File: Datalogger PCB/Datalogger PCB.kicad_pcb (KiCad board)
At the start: 2 copper layers, 9 parts, among them J1 Conn_01x02_Pin, U2 W25Q128JVS

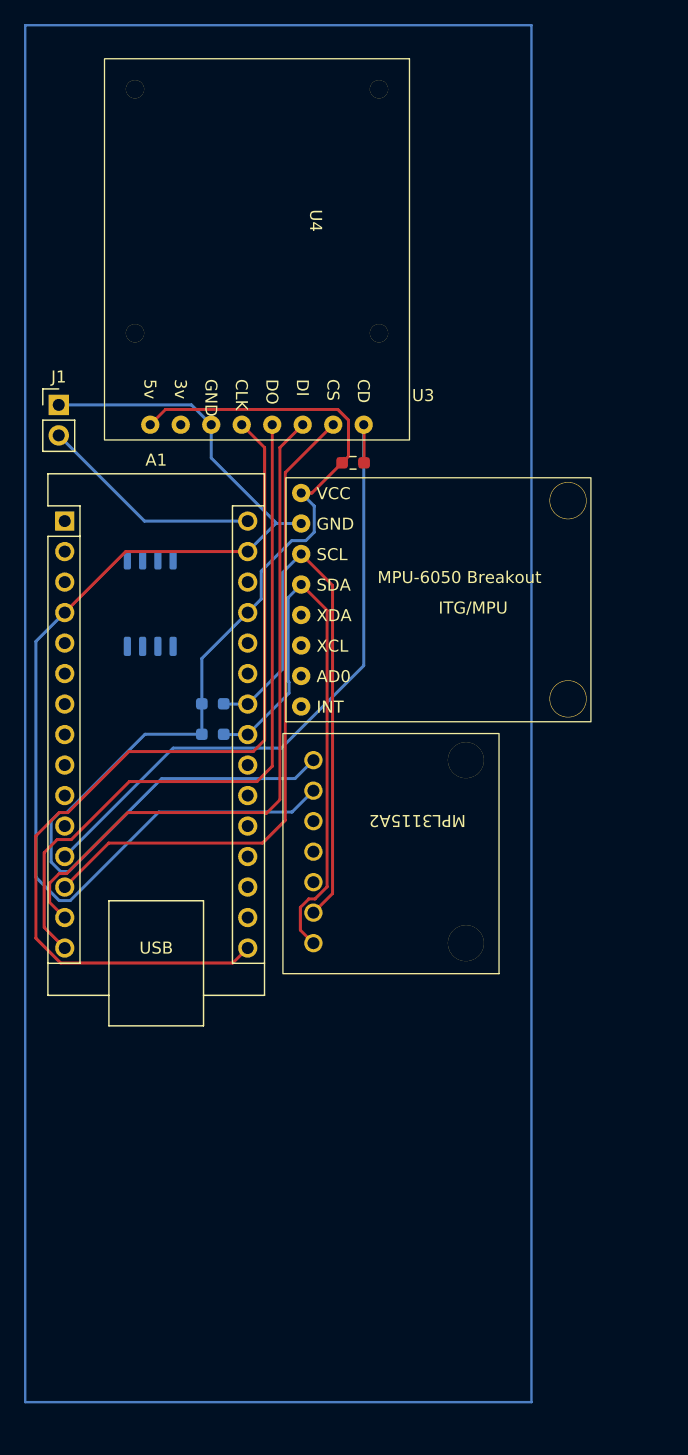
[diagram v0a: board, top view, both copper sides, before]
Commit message: Turn Schematic into PCB
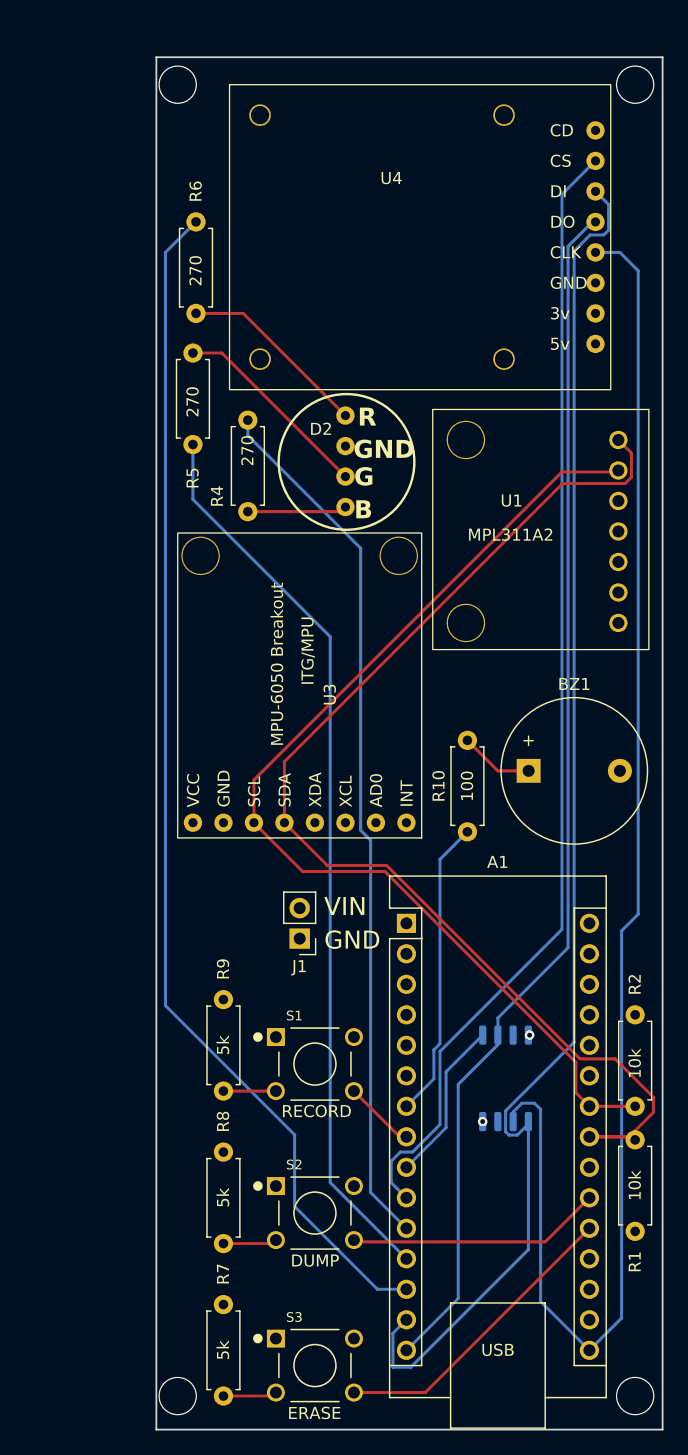
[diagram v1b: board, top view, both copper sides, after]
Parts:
- removed R3: 10k, Resistor_SMD:R_0603_1608Metric_Pad0.98x0.95mm_HandSolder
- added BZ1: Buzzer, Buzzer_Beeper:Buzzer_12x9.5RM7.6, F.Cu at (102.9, 82.5)
- added D2: LED_RKGB, Breakout Boards:RGB_LED, F.Cu at (87.6, 53.0)
- added R10: 100, Resistor_THT:R_Axial_DIN0207_L6.3mm_D2.5mm_P7.62mm_Horizontal, F.Cu at (97.8, 87.6)
- added R4: 270, Resistor_THT:R_Axial_DIN0207_L6.3mm_D2.5mm_P7.62mm_Horizontal, F.Cu at (79.5, 53.3)
- added R5: 270, Resistor_THT:R_Axial_DIN0207_L6.3mm_D2.5mm_P7.62mm_Horizontal, F.Cu at (74.9, 55.4)
- added R6: 270, Resistor_THT:R_Axial_DIN0207_L6.3mm_D2.5mm_P7.62mm_Horizontal, F.Cu at (75.2, 36.8)
- added R7: 5k, Resistor_THT:R_Axial_DIN0207_L6.3mm_D2.5mm_P7.62mm_Horizontal, F.Cu at (77.5, 127.0)
- added R8: 5k, Resistor_THT:R_Axial_DIN0207_L6.3mm_D2.5mm_P7.62mm_Horizontal, F.Cu at (77.5, 114.3)
- added R9: 5k, Resistor_THT:R_Axial_DIN0207_L6.3mm_D2.5mm_P7.62mm_Horizontal, F.Cu at (77.5, 101.6)
- added S1: FSM8JH, Push Button:SW_FSM8JH, F.Cu at (85.1, 107.0)
- added S2: FSM8JH, Push Button:SW_FSM8JH, F.Cu at (85.1, 119.4)
- added S3: FSM8JH, Push Button:SW_FSM8JH, F.Cu at (85.1, 132.1)
- R1, R2: footprint Resistor_SMD:R_0603_1608Metric_Pad0.98x0.95mm_HandSolder -> Resistor_THT:R_Axial_DIN0207_L6.3mm_D2.5mm_P7.62mm_Horizontal; moved to F.Cu
- moved U1 56.0 mm to (112.9, 52.5), turned to 0 degrees
- moved R1 54.3 mm to (111.8, 120.9), turned to 90 degrees
- moved U2 49.4 mm to (101.0, 108.2)
- moved J1 48.8 mm to (83.8, 96.5), turned to 180 degrees
- moved A1 44.0 mm to (92.7, 95.2)
- moved R2 43.7 mm to (111.8, 102.9), turned to -90 degrees
- moved U3 36.6 mm to (67.3, 76.7), turned to 90 degrees
- moved U4 31.2 mm to (108.5, 29.2), turned to 0 degrees
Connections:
- A1 pad 10: unconnected-(A1-D7-Pad10) -> SD_CS
- A1 pad 11: unconnected-(A1-D8-Pad11) -> RGB-B
- A1 pad 12: SD_CD -> RGB-G
- A1 pad 13: SD_CS -> RGB-R
- A1 pad 14: SD_DI -> DI
- A1 pad 15: SD_DO -> DO
- A1 pad 16: SD_CLK -> CLK
- A1 pad 20: unconnected-(A1-A1-Pad20) -> ERASE_BTN
- A1 pad 21: unconnected-(A1-A2-Pad21) -> DUMP_BTN
- A1 pad 7: unconnected-(A1-D4-Pad7) -> Net-(A1-D4)
- A1 pad 8: unconnected-(A1-D5-Pad8) -> RECORD_BTN
- A1 pad 9: unconnected-(A1-D6-Pad9) -> FLASH_CS
- U2 pad 1: unconnected-(U2-~{CS}-Pad1) -> FLASH_CS
- U2 pad 2: unconnected-(U2-DO(IO1)-Pad2) -> DO
- U2 pad 4: unconnected-(U2-GND-Pad4) -> GND
- U2 pad 5: unconnected-(U2-DI(IO0)-Pad5) -> DI
- U2 pad 6: unconnected-(U2-CLK-Pad6) -> CLK
- U2 pad 8: unconnected-(U2-VCC-Pad8) -> +3V3
- U4 pad 1: SD_CD -> unconnected-(U4-CD-Pad1)
- U4 pad 3: SD_DI -> DI
- U4 pad 4: SD_DO -> DO
- U4 pad 5: SD_CLK -> CLK
- U4 pad 7: unconnected-(U4-3v-Pad7) -> +3V3
- U4 pad 8: +5V -> unconnected-(U4-5v-Pad8)
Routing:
- net CLK: track 0.00 -> 121.1 mm
- net DI: track 0.00 -> 116.0 mm
- net +3V3: track 0.00 -> 108.2 mm, vias 0 -> 1
- net DO: track 0.00 -> 100.7 mm
- net RGB-R: track 0.00 -> 99.7 mm
- net GND: track 97.4 -> 0.00 mm, vias 0 -> 1
- net +5V: track 96.2 -> 0.00 mm
- net SD_CLK: track 76.9 -> 0.00 mm
- net RGB-G: track 0.00 -> 75.2 mm
- net RGB-B: track 0.00 -> 72.8 mm
- net SD_DO: track 59.1 -> 0.00 mm
- net SD_DI: track 57.5 -> 0.00 mm
- net SD_CD: track 54.7 -> 0.00 mm
- net SDA: track 48.9 -> 98.9 mm
- net SCL: track 48.0 -> 87.6 mm
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- added copper zone on In1.Cu, net +5V
- added copper zone on In2.Cu, net GND
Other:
- board outline added: 42.2 x 114.3 mm
- copper layers 2 -> 4
- board text added: "DUMP"
- board text added: "ERASE"
- board text added: "GND"
- board text added: "MPL311A2"
- board text added: "PCB need be 1.66 inch by 4.5 inch, 42.164x114.3mm"
- board text added: "RECORD"
- board text added: "VIN"

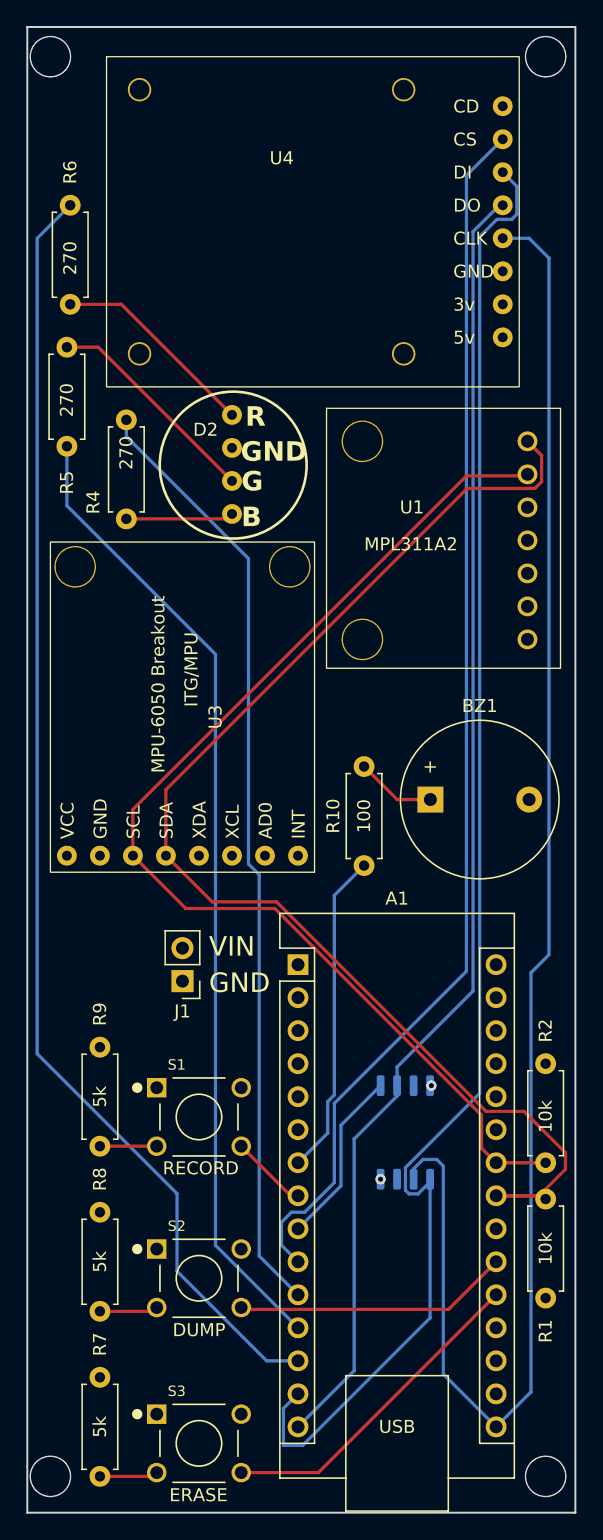
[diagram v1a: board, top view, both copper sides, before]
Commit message: Made board smaller (about 1.6x4inch)
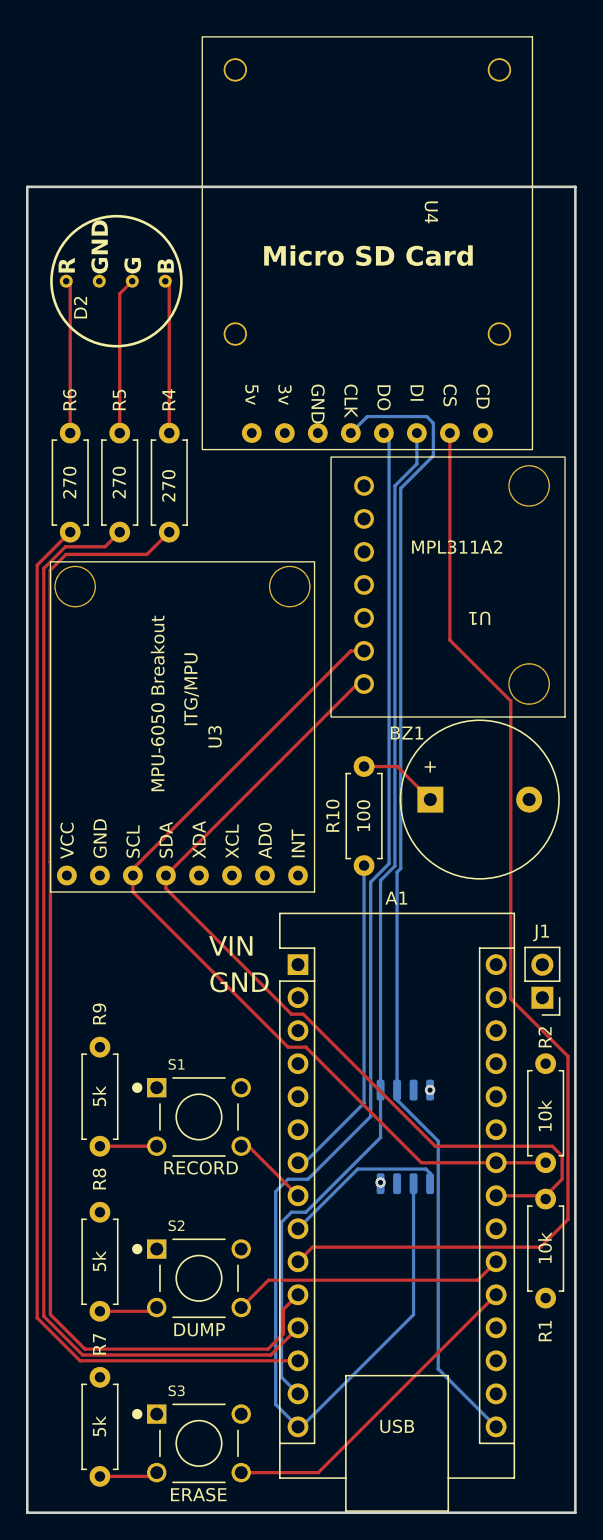
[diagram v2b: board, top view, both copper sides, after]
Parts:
- moved U1 29.6 mm to (95.2, 76.2), turned to 180 degrees
- moved J1 27.7 mm to (111.5, 97.8)
- moved U4 25.2 mm to (106.9, 54.4), turned to -90 degrees
- moved R6 25.1 mm to (75.2, 62.0), turned to 90 degrees
- moved D2 16.4 mm to (74.9, 42.7), turned to 90 degrees
- moved R4 9.25 mm to (82.8, 62.0), turned to 90 degrees
- moved R5 7.75 mm to (79.0, 62.0)
- moved U3 1.52 mm to (67.3, 78.2)
- moved U2 0.34 mm to (101.0, 108.5), turned to 90 degrees
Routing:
- net DI: track 116.0 -> 79.4 mm
- net CLK: track 121.1 -> 88.6 mm
- net SDA: track 98.9 -> 68.8 mm
- net Net-(A1-VIN): track 24.7 -> 3.77 mm
- net SCL: track 87.6 -> 66.9 mm
- net RGB-B: track 72.8 -> 90.6 mm
- net RGB-R: track 99.7 -> 82.9 mm
- net RGB-G: track 75.2 -> 86.2 mm
- net SD_CS: track 94.5 -> 86.4 mm
- net +3V3: track 108.2 -> 100.1 mm
- net Net-(D2-GA): track 17.0 -> 12.1 mm
- net Net-(D2-RA): track 16.0 -> 11.8 mm
- net DO: track 100.7 -> 104.4 mm
- net Net-(D2-BA): track 8.29 -> 11.8 mm
- net FLASH_CS: track 13.6 -> 13.0 mm
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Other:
- board size 42.2 x 114.3 mm -> 42.2 x 102 mm
- board text added: "Micro SD Card"

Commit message: Added Test
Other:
- board text added: "+"
- board text added: "Datalogger v1"
- board text added: "Developed By Pioneer Rocketry"
- board text removed: "GND"
- board text removed: "VIN"

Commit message: Added logo to PCB
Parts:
- added G***: LOGO, Breakout Boards:Logo, F.Cu at (82.9, 96.6)

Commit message: V2 pcb (#19)
Completed PCB design
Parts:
- removed A1: Arduino_Nano_v3.x, Module:Arduino_Nano
- removed S1, S2, S3: FSM8JH, Push Button:SW_FSM8JH
- added C1: 0.1uF, Resistor_SMD:R_0603_1608Metric_Pad0.98x0.95mm_HandSolder, F.Cu at (154.7, 57.8)
- added C2: 0.1uF, Resistor_SMD:R_0603_1608Metric_Pad0.98x0.95mm_HandSolder, F.Cu at (159.1, 65.9)
- added C3: .12uF, Resistor_SMD:R_0603_1608Metric_Pad0.98x0.95mm_HandSolder, F.Cu at (155.9, 69.8)
- added C4: 1uF, Resistor_SMD:R_0603_1608Metric_Pad0.98x0.95mm_HandSolder, F.Cu at (160.5, 72.6)
- added C5: 10uF, Resistor_SMD:R_0603_1608Metric_Pad0.98x0.95mm_HandSolder, B.Cu at (143.4, 128.5)
- added C6: 22uF, Resistor_SMD:R_0603_1608Metric_Pad0.98x0.95mm_HandSolder, B.Cu at (145.8, 128.5)
- added D1: LED_GBAR, Led:LED_GBAR, F.Cu at (143.2, 132.5)
- added H1: MountingHole, MountingHole:MountingHole_2.2mm_M2, F.Cu at (140.0, 44.7)
- added H2: MountingHole, MountingHole:MountingHole_2.2mm_M2, F.Cu at (177.2, 44.7)
- added H3: MountingHole, MountingHole:MountingHole_2.2mm_M2, F.Cu at (177.2, 141.5)
- added H4: MountingHole, MountingHole:MountingHole_2.2mm_M2, F.Cu at (140.0, 141.5)
- added I2C1: Conn_02x02_Counter_Clockwise, Connector_PinHeader_1.27mm:PinHeader_2x02_P1.27mm_Vertical, F.Cu at (176.5, 118.2)
- added M1: Motor_Servo, Connector_PinHeader_2.54mm:PinHeader_1x03_P2.54mm_Vertical, F.Cu at (142.1, 55.4)
- added M2: Motor_Servo, Connector_PinHeader_2.54mm:PinHeader_1x03_P2.54mm_Vertical, F.Cu at (142.1, 49.0)
- added M3: Motor_Servo, Connector_PinHeader_2.54mm:PinHeader_1x03_P2.54mm_Vertical, F.Cu at (171.5, 55.4)
- added M4: Motor_Servo, Connector_PinHeader_2.54mm:PinHeader_1x03_P2.54mm_Vertical, F.Cu at (171.5, 49.0)
- added PYRO_1-2: Screw_Terminal_01x04, TerminalBlock:TerminalBlock_bornier-4_P5.08mm, F.Cu at (141.5, 63.1)
- added PYRO_3-4: Screw_Terminal_01x04, TerminalBlock:TerminalBlock_bornier-4_P5.08mm, F.Cu at (175.8, 77.8)
- added PYRO_SWITCH1: Screw_Terminal_01x02, TerminalBlock:TerminalBlock_bornier-2_P5.08mm, F.Cu at (141.5, 84.0)
- added Power1: Conn_01x04_Pin, Connector_PinHeader_1.27mm:PinHeader_1x04_P1.27mm_Vertical, F.Cu at (140.8, 134.2)
- added R11: 10k, Resistor_SMD:R_0603_1608Metric_Pad0.98x0.95mm_HandSolder, F.Cu at (154.9, 67.1)
- added R12: 10k, Resistor_SMD:R_0603_1608Metric_Pad0.98x0.95mm_HandSolder, B.Cu at (152.0, 135.0)
- added R13: 2k, Resistor_SMD:R_0603_1608Metric_Pad0.98x0.95mm_HandSolder, B.Cu at (152.0, 130.4)
- added R14: 10k, Resistor_SMD:R_0603_1608Metric_Pad0.98x0.95mm_HandSolder, B.Cu at (174.8, 95.5)
- added R15: 10k, Resistor_SMD:R_0603_1608Metric_Pad0.98x0.95mm_HandSolder, B.Cu at (174.8, 100.8)
- added R3: 100, Resistor_SMD:R_0603_1608Metric_Pad0.98x0.95mm_HandSolder, F.Cu at (147.9, 133.3)
- added RECORD_BTN1: FSM8JH, Push Button:SW_FSM8JH, F.Cu at (147.2, 108.3)
- added SPI1: Conn_02x04_Counter_Clockwise, Connector_PinHeader_1.27mm:PinHeader_2x04_P1.27mm_Vertical, F.Cu at (176.4, 124.5)
- added Serial1: Conn_01x04_Pin, Connector_PinHeader_1.27mm:PinHeader_1x04_P1.27mm_Vertical, F.Cu at (177.0, 136.7)
- added U5: NRF24L01_Breakout, RF_Module:nRF24L01_Breakout, F.Cu at (153.9, 52.6)
- added U6: VN5E160STR-E, SOIC127P600X175-8N:SOIC127P600X175-8N, B.Cu at (147.1, 65.7)
- added U7: VN5E160STR-E, SOIC127P600X175-8N:SOIC127P600X175-8N, B.Cu at (147.1, 75.8)
- added U8: VN5E160STR-E, SOIC127P600X175-8N:SOIC127P600X175-8N, B.Cu at (170.3, 75.2)
- added U9: VN5E160STR-E, SOIC127P600X175-8N:SOIC127P600X175-8N, B.Cu at (170.2, 65.1)
- D2: value LED_RKGB -> D; footprint Breakout Boards:RGB_LED -> Diode_SMD:D_0603_1608Metric_Pad1.05x0.95mm_HandSolder; moved to B.Cu
- R1, R2: value 10k -> 100; footprint Resistor_THT:R_Axial_DIN0207_L6.3mm_D2.5mm_P7.62mm_Horizontal -> Resistor_SMD:R_0603_1608Metric_Pad0.98x0.95mm_HandSolder
- R10: value 100 -> 10k; footprint Resistor_THT:R_Axial_DIN0207_L6.3mm_D2.5mm_P7.62mm_Horizontal -> Resistor_SMD:R_0603_1608Metric_Pad0.98x0.95mm_HandSolder
- R4, R5: value 270 -> 10k; footprint Resistor_THT:R_Axial_DIN0207_L6.3mm_D2.5mm_P7.62mm_Horizontal -> Resistor_SMD:R_0603_1608Metric_Pad0.98x0.95mm_HandSolder; moved to B.Cu
- R6: value 270 -> 5.1k; footprint Resistor_THT:R_Axial_DIN0207_L6.3mm_D2.5mm_P7.62mm_Horizontal -> Resistor_SMD:R_0603_1608Metric_Pad0.98x0.95mm_HandSolder
- R7: value 5k -> 100; footprint Resistor_THT:R_Axial_DIN0207_L6.3mm_D2.5mm_P7.62mm_Horizontal -> Resistor_SMD:R_0603_1608Metric_Pad0.98x0.95mm_HandSolder
- R8, R9: value 5k -> 10k; footprint Resistor_THT:R_Axial_DIN0207_L6.3mm_D2.5mm_P7.62mm_Horizontal -> Resistor_SMD:R_0603_1608Metric_Pad0.98x0.95mm_HandSolder
- U1: value ~ -> Teensy4.1; footprint Breakout Boards:MPL3115A2 -> Teensy4.1:Teensy41
- U2: value W25Q128JVS -> BNO055; footprint Package_SO:SOIC-8_5.23x5.23mm_P1.27mm -> Package_LGA:LGA-28_5.2x3.8mm_P0.5mm; moved to F.Cu
- U3: value ~ -> LPS25HB; footprint Datalogging Breakout:MPU-6050 Breakout -> Package_LGA:ST_HLGA-10_2.5x2.5mm_P0.6mm_LayoutBorder3x2y
- U4: value ~ -> AMS1117-5.0; footprint Breakout Boards:Adafruit Micro-SD Breakout Board+ -> Package_TO_SOT_SMD:SOT-223-3_TabPin2; moved to B.Cu
- moved D2 112.4 mm to (148.6, 127.5), turned to -90 degrees
- moved U3 93.2 mm to (158.5, 59.3), turned to 0 degrees
- moved U4 90.0 mm to (145.7, 135.5)
- moved R5 88.5 mm to (160.0, 97.5), turned to 180 degrees
- moved R4 86.4 mm to (160.0, 100.8), turned to 180 degrees
- moved R6 81.3 mm to (140.4, 110.5), turned to 0 degrees
- moved R9 77.7 mm to (152.7, 121.0), turned to 0 degrees
- moved U1 77.5 mm to (163.9, 112.1), turned to 90 degrees
- moved R8 75.8 mm to (152.7, 123.6), turned to 0 degrees
- moved R7 75.5 mm to (152.3, 116.7), turned to 180 degrees
- moved U2 70.9 mm to (160.2, 69.4), turned to 0 degrees
- moved G*** 64.5 mm to (147.4, 96.6)
- moved R10 63.4 mm to (160.0, 75.5), turned to 0 degrees
- moved J1 59.0 mm to (150.6, 142.0), turned to -90 degrees
- moved BZ1 54.3 mm to (140.0, 122.2)
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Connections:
- D2 pad 1: Net-(D2-RA) -> +5V
- D2 pad 2: GND -> Net-(D2-A)
- J1 pad 2: Net-(A1-VIN) -> /VIN
- R1 pad 1: +5V -> /RGB-R
- R1 pad 2: SDA -> Net-(D1-RK)
- R10 pad 1: Net-(A1-D4) -> +3.3V
- R10 pad 2: Net-(BZ1--) -> Net-(U2-~{RESET})
- R2 pad 1: +5V -> /RGB-G
- R2 pad 2: SCL -> Net-(D1-GK)
- R4 pad 1: RGB-B -> GND
- R4 pad 2: Net-(D2-BA) -> /PYRO_2
- R5 pad 1: RGB-G -> GND
- R5 pad 2: Net-(D2-GA) -> /PYRO_1
- R6 pad 1: RGB-R -> GND
- R6 pad 2: Net-(D2-RA) -> Net-(R6-Pad2)
- R7 pad 1: GND -> Net-(U1-17_A3_TX4_SDA1)
- R7 pad 2: Net-(R7-Pad2) -> Net-(BZ1--)
- R8 pad 1: GND -> +3.3V
- R8 pad 2: Net-(R8-Pad2) -> /SCL
- R9 pad 1: GND -> +3.3V
- R9 pad 2: Net-(R9-Pad2) -> /SDA
- U1 pad 1: SDA -> GND
- U1 pad 2: SCL -> /RX
- U1 pad 3: unconnected-(U1-INT1-Pad3) -> /TX
- U1 pad 4: unconnected-(U1-INT2-Pad4) -> /RGB-G
- U1 pad 6: GND -> /EXTERNAL_CS3
- U1 pad 7: +5V -> /EXTERNAL_CS2
- U1 pad 8: (no net) -> /EXTERNAL_CS1
- U1 pad 9: (no net) -> unconnected-(U1-7_RX2_OUT1A-Pad9)
- U2 pad 1: FLASH_CS -> unconnected-(U2-PIN1-Pad1)
- U2 pad 2: DO -> GND
- U2 pad 3: unconnected-(U2-IO2-Pad3) -> +3.3V
- U2 pad 4: GND -> Net-(U2-~{BOOT_LOAD_PIN})
- U2 pad 5: DI -> GND
- U2 pad 6: CLK -> GND
- U2 pad 8: +3V3 -> unconnected-(U2-PIN8-Pad8)
- U3 pad 1: +5V -> +3.3V
- U3 pad 10: (no net) -> +3.3V
- U3 pad 2: GND -> /SCL
- U3 pad 3: SCL -> unconnected-(U3-RES-Pad3)
- U3 pad 4: SDA -> /SDA
- U3 pad 6: unconnected-(U3-XDL-Pad6) -> +3.3V
- U3 pad 8: unconnected-(U3-INT-Pad8) -> GND
- U3 pad 9: (no net) -> GND
- U4 pad 1: unconnected-(U4-CD-Pad1) -> GND
- U4 pad 2: SD_CS -> Net-(D2-A)
- U4 pad 3: DI -> /VIN
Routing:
- net +5V: track 0.00 -> 161.4 mm
- net DO: track 104.4 -> 0.00 mm
- net /SDA: track 0.00 -> 100.7 mm
- net /SCL: track 0.00 -> 100.2 mm, vias 0 -> 3
- net +3V3: track 100.1 -> 0.00 mm, vias 1 -> 0
- net /CLK: track 0.00 -> 93.6 mm
- net RGB-B: track 90.6 -> 0.00 mm
- net CLK: track 88.6 -> 0.00 mm
- net /PYRO_POWER: track 0.00 -> 87.4 mm, vias 0 -> 8
- net /DI: track 0.00 -> 87.2 mm
- net SD_CS: track 86.4 -> 0.00 mm
- net RGB-G: track 86.2 -> 0.00 mm
- net /DO: track 0.00 -> 84.2 mm, vias 0 -> 2
- net RGB-R: track 82.9 -> 0.00 mm
- net DI: track 79.4 -> 0.00 mm
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- added copper zone on B.Cu, net +3.3V
- added copper zone on In2.Cu, net +3.3V
- added copper zone on F.Cu, net GND
- added copper zone on In1.Cu, net GND
- removed copper zone on In1.Cu, net +5V
- removed copper zone on In2.Cu, net GND
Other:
- board size 42.2 x 102 mm -> 42.2 x 101.8 mm
- board text added: "+ CS1 CS2 CS3"
- board text added: "+ SCL"
- board text added: "-"
- board text added: "- TX RX +"
- board text added: "3.3 VIN 5v -"
- board text added: "CH 1"
- board text added: "CH 2"
- board text added: "CH 3"
- board text added: "CH 4"
- board text added: "DI GND"
- board text added: "DO CLK"
- board text added: "Pioneer Rocketry Datalogger v2.1"
- board text added: "SDA"
- board text added: "Signal + -"
- board text removed: "DUMP"
- board text removed: "Datalogger v1"
- board text removed: "Developed By Pioneer Rocketry"
- board text removed: "ERASE"
- board text removed: "MPL311A2"
- board text removed: "Micro SD Card"
- board text removed: "RECORD"
